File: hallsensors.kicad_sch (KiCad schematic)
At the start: 23 parts

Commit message: Fixes, layouting
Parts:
- removed C49, C51: 10uF, Capacitor_SMD:C_0603_1608Metric_Pad1.08x0.95mm_HandSolder, symbol Device:C
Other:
- moved on the sheet: C50, C52

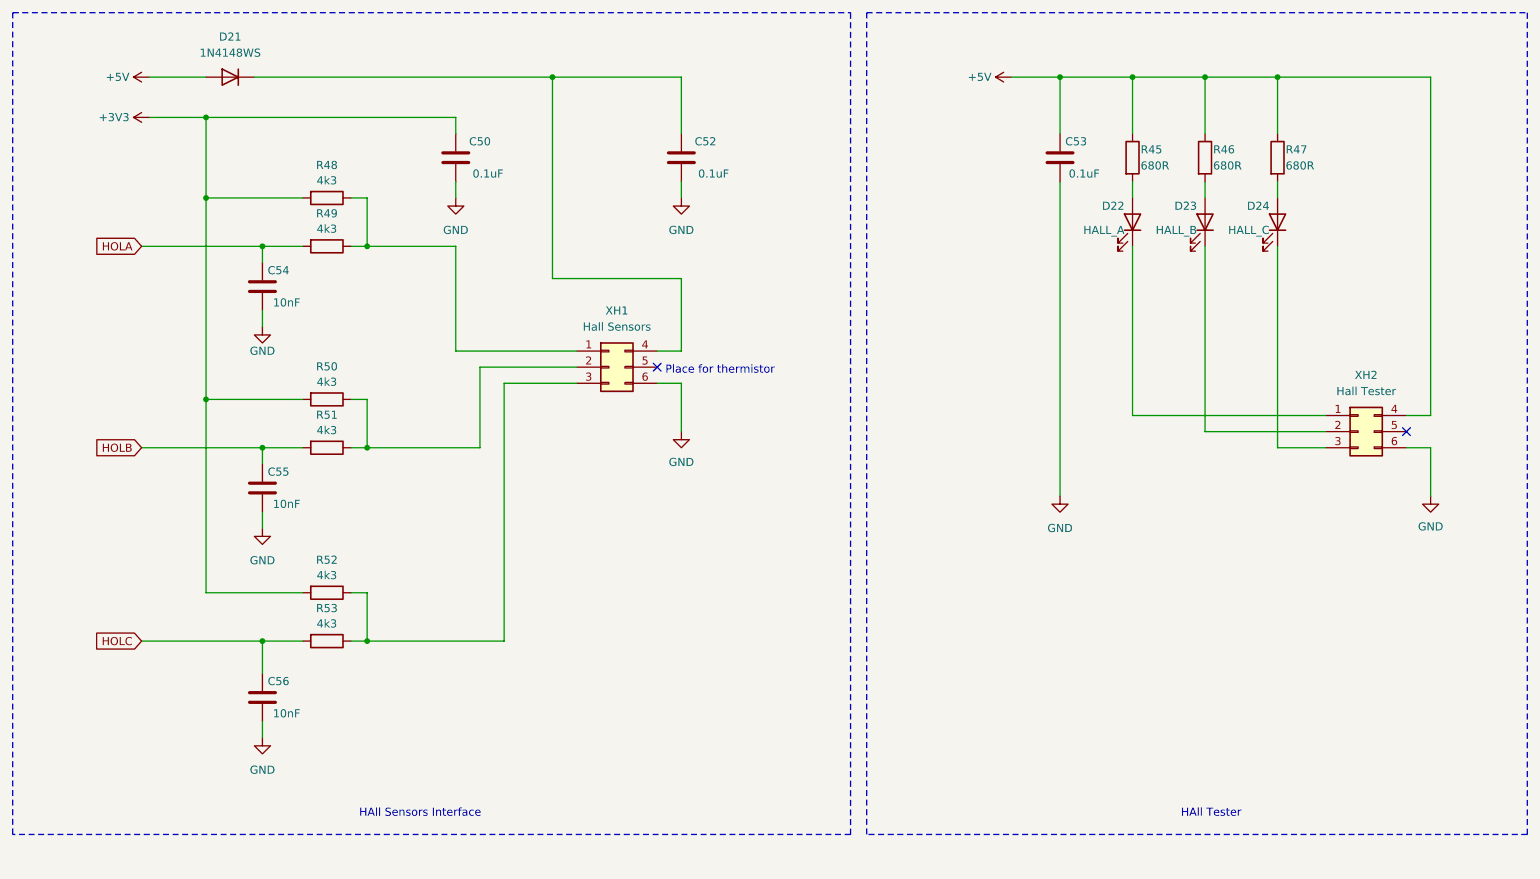
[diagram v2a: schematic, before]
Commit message: Major update on results of testing first order board and on results of crosscheck
* reworked mainswitch scheme
* mainswitch divider. expected commutation time - 2us
* added 3v3bt and 3v3hall
* tvs on hall
* divided 5vhall, 3vhall, 3vbt
* fix misplacement gnd and 3v3 at the BT connector
* fix motorbut (now pullup and gnd on button)
* fix opto gate

+ a lot of minors
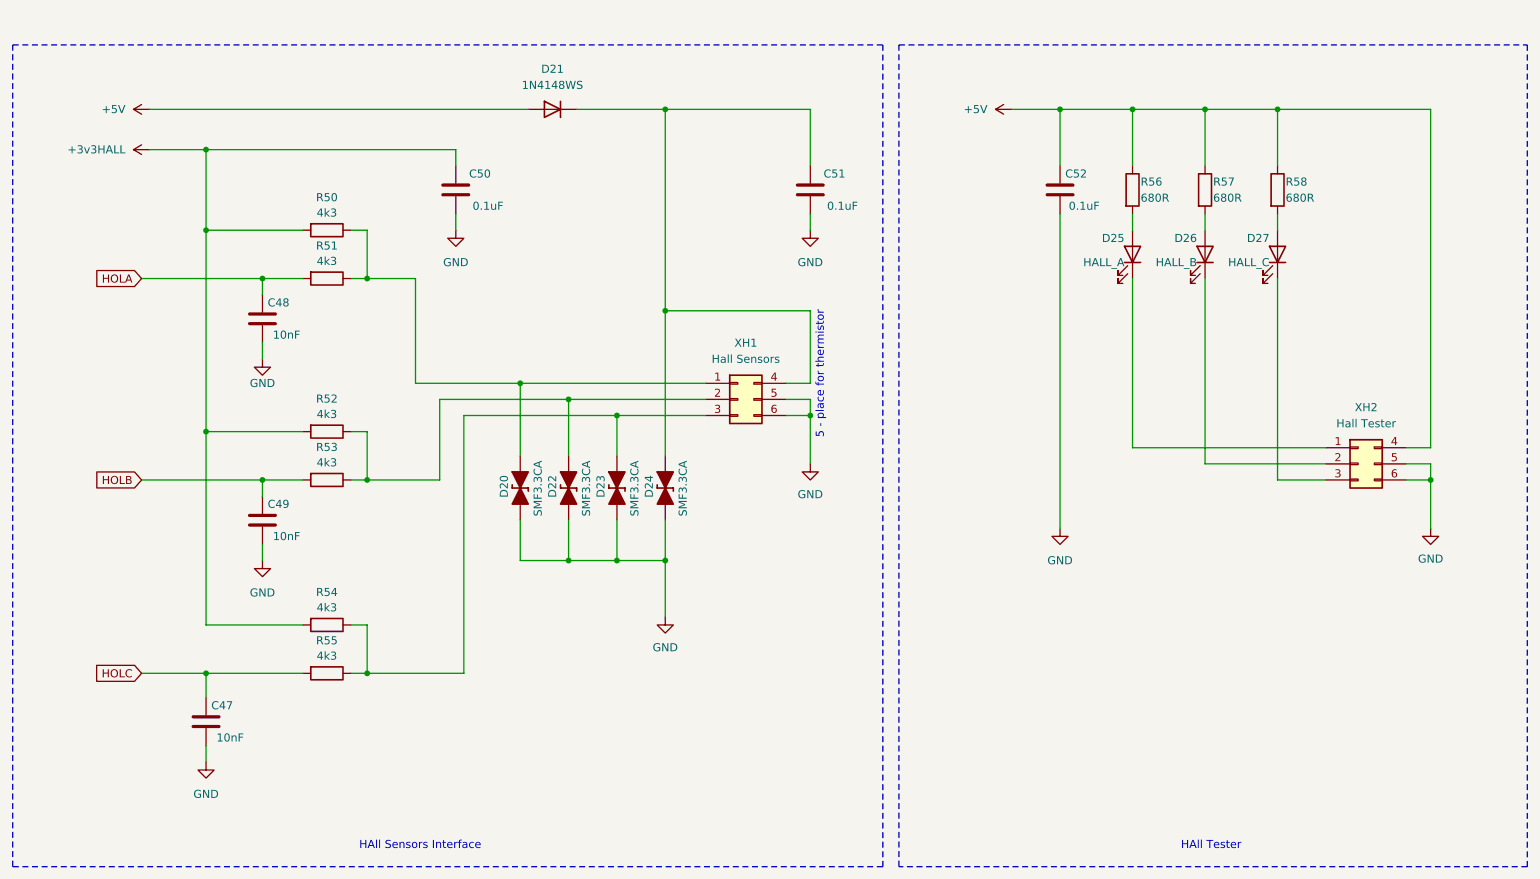
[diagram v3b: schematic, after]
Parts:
- added D20, D22, D23, D24: SMF3.3CA, Diode_SMD_AKL:D_SOD-123F, symbol 4shift:SMF3.3CA
- renumbered C56 to C47, C54 to C48, C55 to C49, C52 to C51, C53 to C52, D22 to D25, D23 to D26, D24 to D27, R48 to R50, R49 to R51, R50 to R52, R51 to R53, R52 to R54, R53 to R55, R45 to R56, R46 to R57, R47 to R58
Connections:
- net GND: now also XH1.5 (Pin_5), XH2.5 (Pin_5), D20.1 (K), D22.1 (K), D23.1 (K), D24.1 (K)
- net at R50.1, R51.1, XH1.1 (Pin_1): now also D20.2 (A)
- net at R52.1, R53.1, XH1.2 (Pin_2): now also D22.2 (A)
- net at R54.1, R55.1, XH1.3 (Pin_3): now also D23.2 (A)
- net at C51.1, D21.1 (K), XH1.4 (Pin_4): now also D24.2 (A)
- net +3V3 renamed +3v3HALL
- no-connect marks 2 -> 0
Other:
- note added: "5 - place for thermistor"
- note removed: "Place for thermistor"
- moved on the sheet: C47, C48, C49, C50, C51, C52, D25, D26, D27, R50, R51, R52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
